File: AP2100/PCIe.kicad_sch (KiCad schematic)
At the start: 8 parts, among them J2 Bus_PCI_Express_Mini, J6 Bus_PCI_Express_Mini

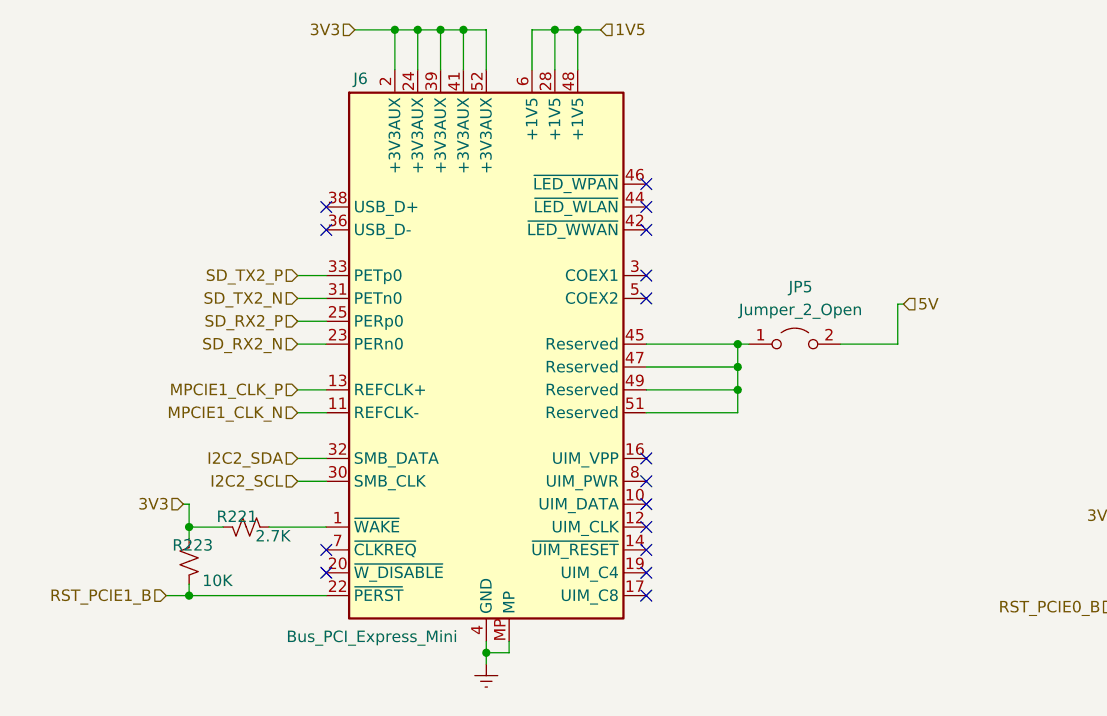
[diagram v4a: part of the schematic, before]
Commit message: RGMII ethernet section almost complete for 1st port Finish USB
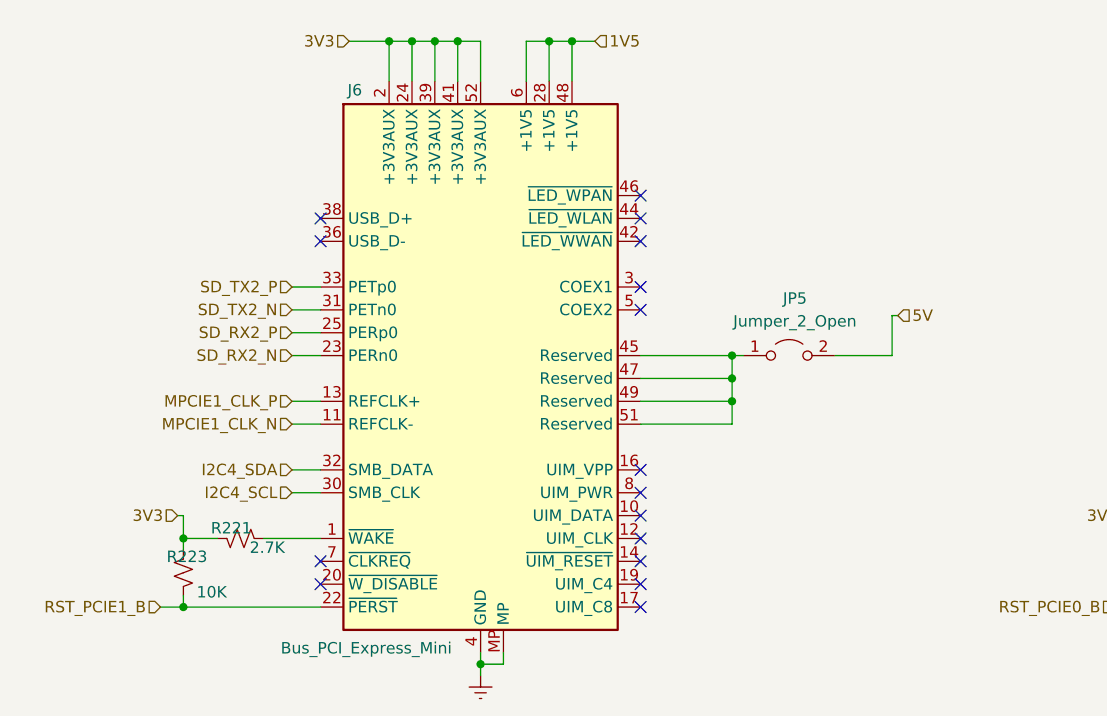
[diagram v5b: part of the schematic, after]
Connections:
- net I2C2_SCL: no longer J6.30 (SMB_CLK)
- net I2C2_SDA: no longer J6.32 (SMB_DATA)
- new net I2C4_SCL: J6.30 (SMB_CLK)
- new net I2C4_SDA: J6.32 (SMB_DATA)
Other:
- moved on the sheet: J6, JP5, R221, R223

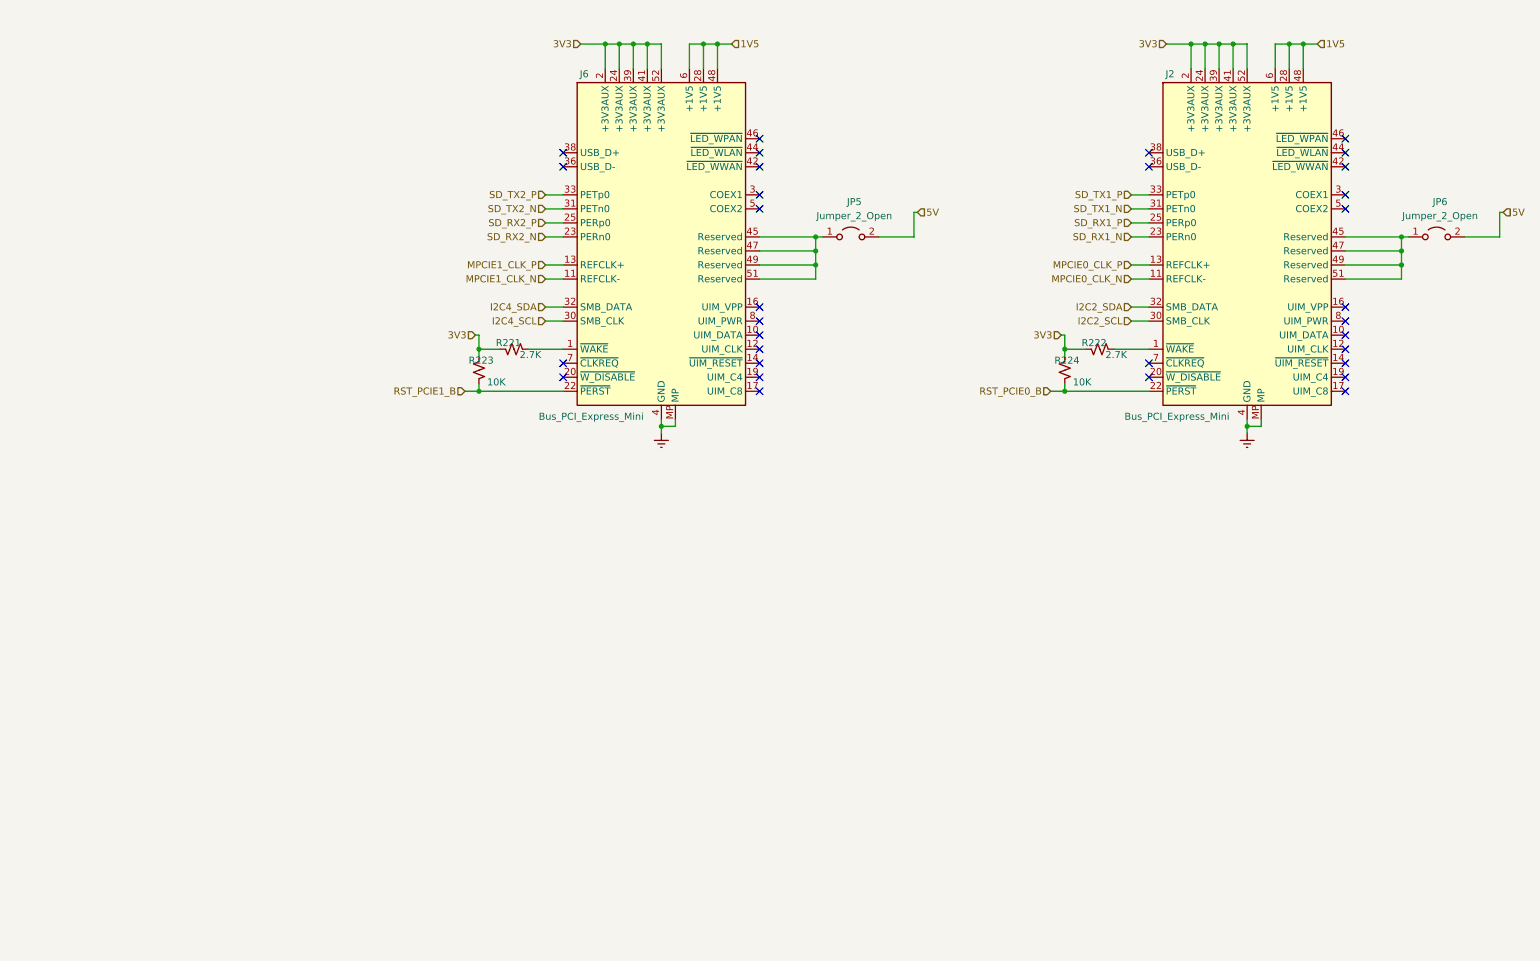
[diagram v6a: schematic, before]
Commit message: Review / cleanup footprints, etc
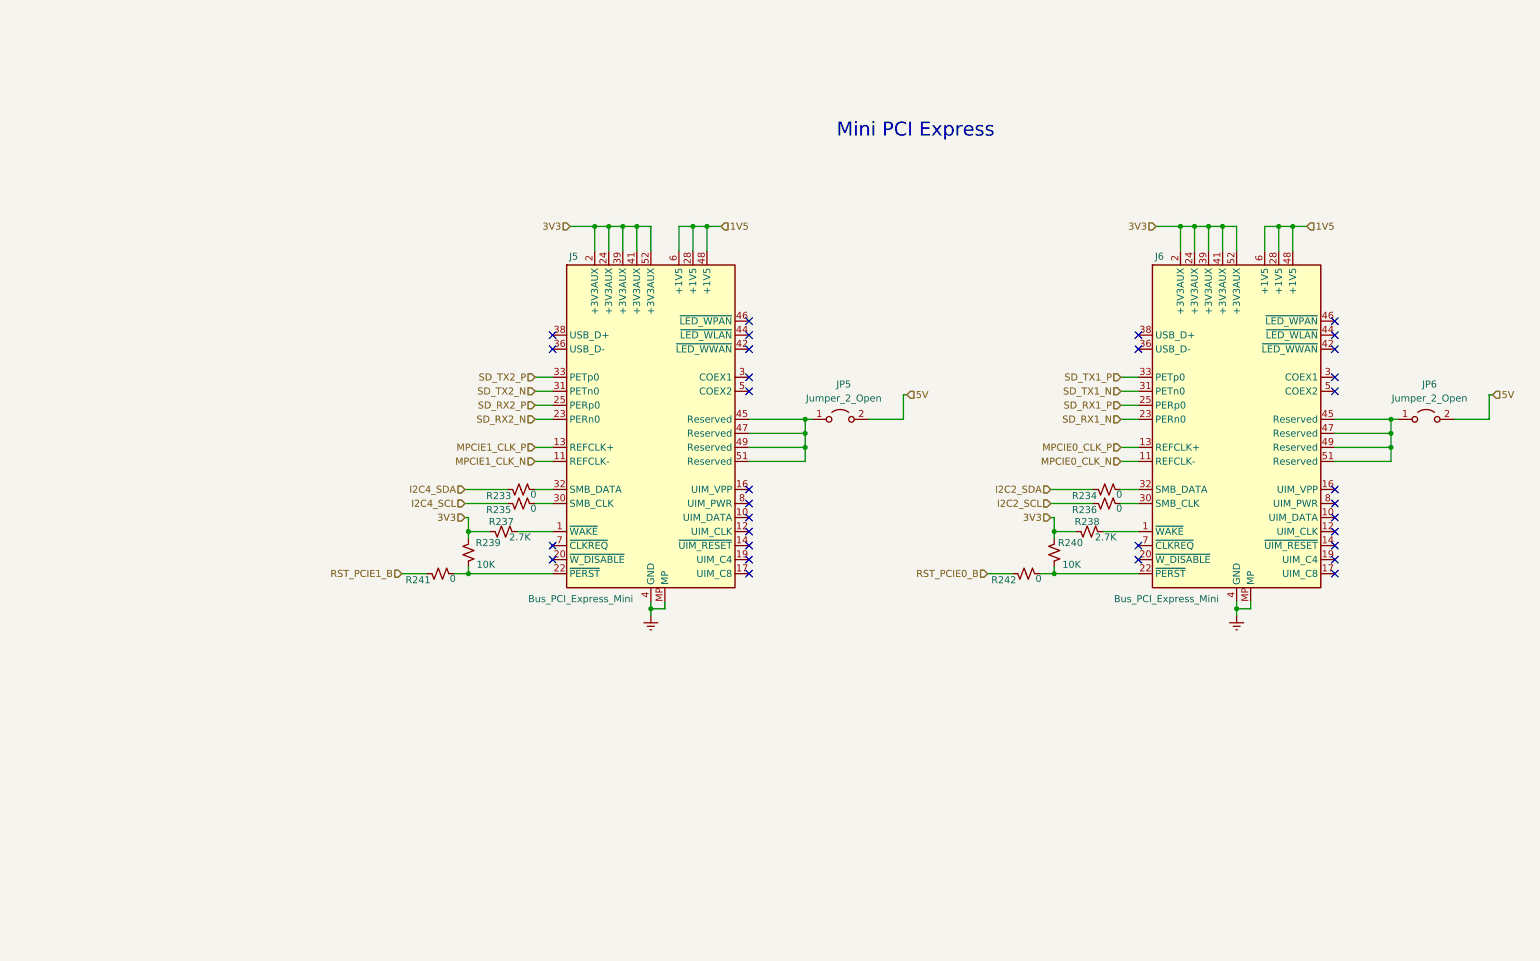
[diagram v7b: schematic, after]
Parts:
- added R233, R234, R235, R236, R241, R242: 0, Resistor_SMD:R_0402_1005Metric, symbol Device:R_Small_US
- renumbered J6 to J5, J2 to J6, R221 to R237, R222 to R238, R223 to R239, R224 to R240
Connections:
- net I2C2_SCL: now also R236.1; no longer J6.30 (SMB_CLK)
- net I2C2_SDA: now also R234.1; no longer J6.32 (SMB_DATA)
- net I2C4_SCL: now also R235.1; no longer J5.30 (SMB_CLK)
- net I2C4_SDA: now also R233.1; no longer J5.32 (SMB_DATA)
- net RST_PCIE0_B: now also R242.1; no longer J6.22 (~PERST), R240.2
- net RST_PCIE1_B: now also R241.1; no longer J5.22 (~PERST), R239.2
- new net: J6.22 (~PERST), R240.2, R242.2
- new net: J6.30 (SMB_CLK), R236.2
- new net: J6.32 (SMB_DATA), R234.2
- new net: J5.32 (SMB_DATA), R233.2
- new net: J5.22 (~PERST), R239.2, R241.2
- new net: J5.30 (SMB_CLK), R235.2
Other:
- note added: "Mini PCI Express"
- moved on the sheet: J5, J6, JP5, JP6, R237, R238, R239, R240

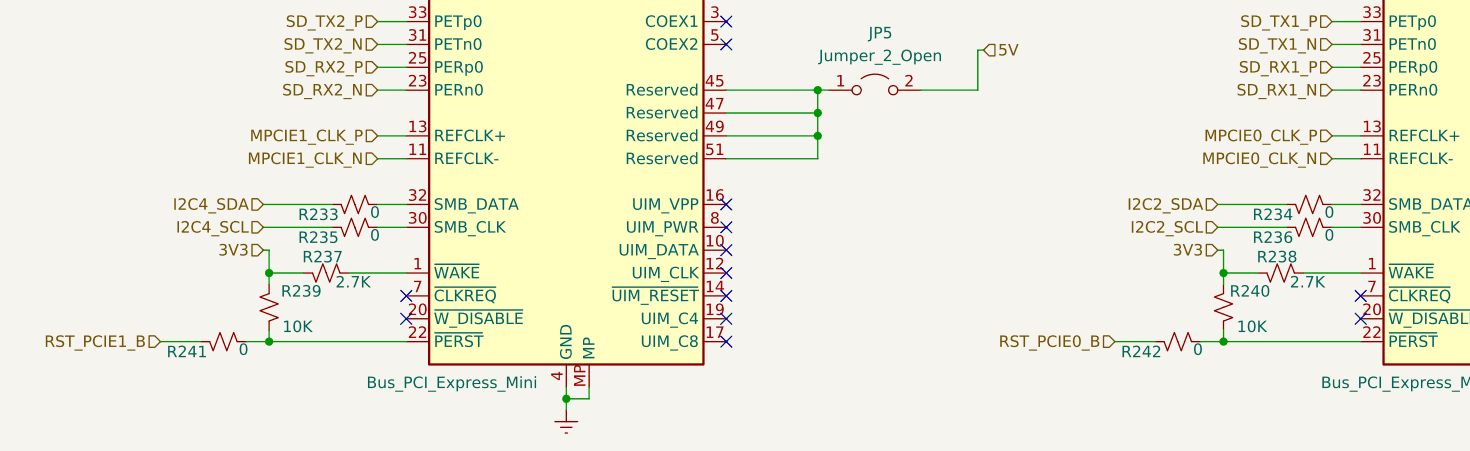
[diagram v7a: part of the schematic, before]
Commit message: Added antenna mounting holes
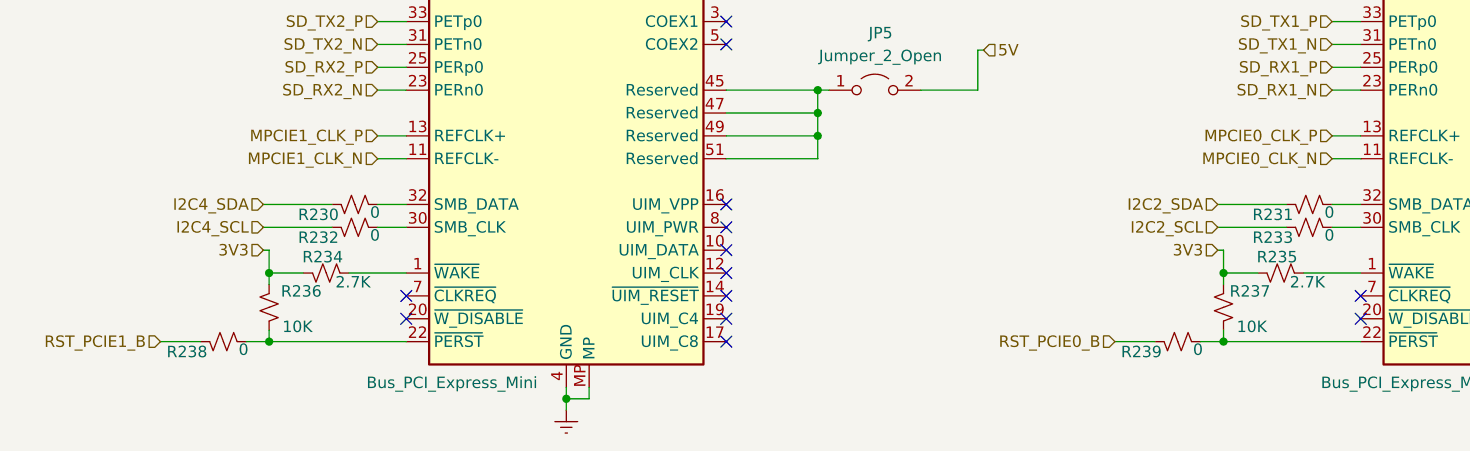
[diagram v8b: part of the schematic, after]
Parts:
- renumbered R233 to R230, R234 to R231, R235 to R232, R236 to R233, R237 to R234, R238 to R235, R239 to R236, R240 to R237, R241 to R238, R242 to R239
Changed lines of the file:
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@@
   (symbol (lib_id "Device:R_Small_US") (at 110.49 127 90) (mirror x) (unit 1)
     (in_bom yes) (on_board yes)
-    (property "Reference" "R241" (id 0) (at 108.712 128.143 90)
+    (property "Reference" "R238" (id 0) (at 108.712 128.143 90)
       (effects (font (size 1.27 1.27)) (justify left))
     )
@@
   (symbol (lib_id "Device:R_Small_US") (at 115.57 123.19 0) (mirror y) (unit 1)
     (in_bom yes) (on_board yes)
-    (property "Reference" "R239" (id 0) (at 121.412 121.412 0)
+    (property "Reference" "R236" (id 0) (at 121.412 121.412 0)
       (effects (font (size 1.27 1.27)) (justify left))
     )
@@
   (symbol (lib_id "Device:R_Small_US") (at 121.92 119.38 270) (mirror x) (unit 1)
     (in_bom yes) (on_board yes)
-    (property "Reference" "R237" (id 0) (at 119.253 117.602 90)
+    (property "Reference" "R234" (id 0) (at 119.253 117.602 90)
       (effects (font (size 1.27 1.27)) (justify left))
     )
@@
   (symbol (lib_id "Device:R_Small_US") (at 125.095 111.76 90) (mirror x) (unit 1)
     (in_bom yes) (on_board yes)
-    (property "Reference" "R233" (id 0) (at 123.317 112.903 90)
+    (property "Reference" "R230" (id 0) (at 123.317 112.903 90)
       (effects (font (size 1.27 1.27)) (justify left))
     )
@@
   (symbol (lib_id "Device:R_Small_US") (at 125.095 114.3 90) (mirror x) (unit 1)
     (in_bom yes) (on_board yes)
-    (property "Reference" "R235" (id 0) (at 123.317 115.443 90)
+    (property "Reference" "R232" (id 0) (at 123.317 115.443 90)
       (effects (font (size 1.27 1.27)) (justify left))
     )
@@
   (symbol (lib_id "Device:R_Small_US") (at 216.535 127 90) (mirror x) (unit 1)
     (in_bom yes) (on_board yes)
-    (property "Reference" "R242" (id 0) (at 214.757 128.143 90)
+    (property "Reference" "R239" (id 0) (at 214.757 128.143 90)
       (effects (font (size 1.27 1.27)) (justify left))
     )
@@
   (symbol (lib_id "Device:R_Small_US") (at 221.615 123.19 0) (mirror y) (unit 1)
     (in_bom yes) (on_board yes)
-    (property "Reference" "R240" (id 0) (at 226.822 121.412 0)
+    (property "Reference" "R237" (id 0) (at 226.822 121.412 0)
       (effects (font (size 1.27 1.27)) (justify left))
     )
@@
   (symbol (lib_id "Device:R_Small_US") (at 227.965 119.38 270) (mirror x) (unit 1)
     (in_bom yes) (on_board yes)
-    (property "Reference" "R238" (id 0) (at 225.298 117.602 90)
+    (property "Reference" "R235" (id 0) (at 225.298 117.602 90)
       (effects (font (size 1.27 1.27)) (justify left))
     )
@@
   (symbol (lib_id "Device:R_Small_US") (at 231.14 111.76 90) (mirror x) (unit 1)
     (in_bom yes) (on_board yes)
-    (property "Reference" "R234" (id 0) (at 229.362 112.903 90)
+    (property "Reference" "R231" (id 0) (at 229.362 112.903 90)
       (effects (font (size 1.27 1.27)) (justify left))
     )
@@
   (symbol (lib_id "Device:R_Small_US") (at 231.14 114.3 90) (mirror x) (unit 1)
     (in_bom yes) (on_board yes)
-    (property "Reference" "R236" (id 0) (at 229.362 115.443 90)
+    (property "Reference" "R233" (id 0) (at 229.362 115.443 90)
       (effects (font (size 1.27 1.27)) (justify left))
     )
